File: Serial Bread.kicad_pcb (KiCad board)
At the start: 2 copper layers, 26 x 32 mm, 24 parts, among them J1 USB_C_Receptacle_USB2.0, J2 Conn_02x04_Top_Bottom, SW1 SW_SPDT, U1 CH340C, U2 AP2112K-3.3

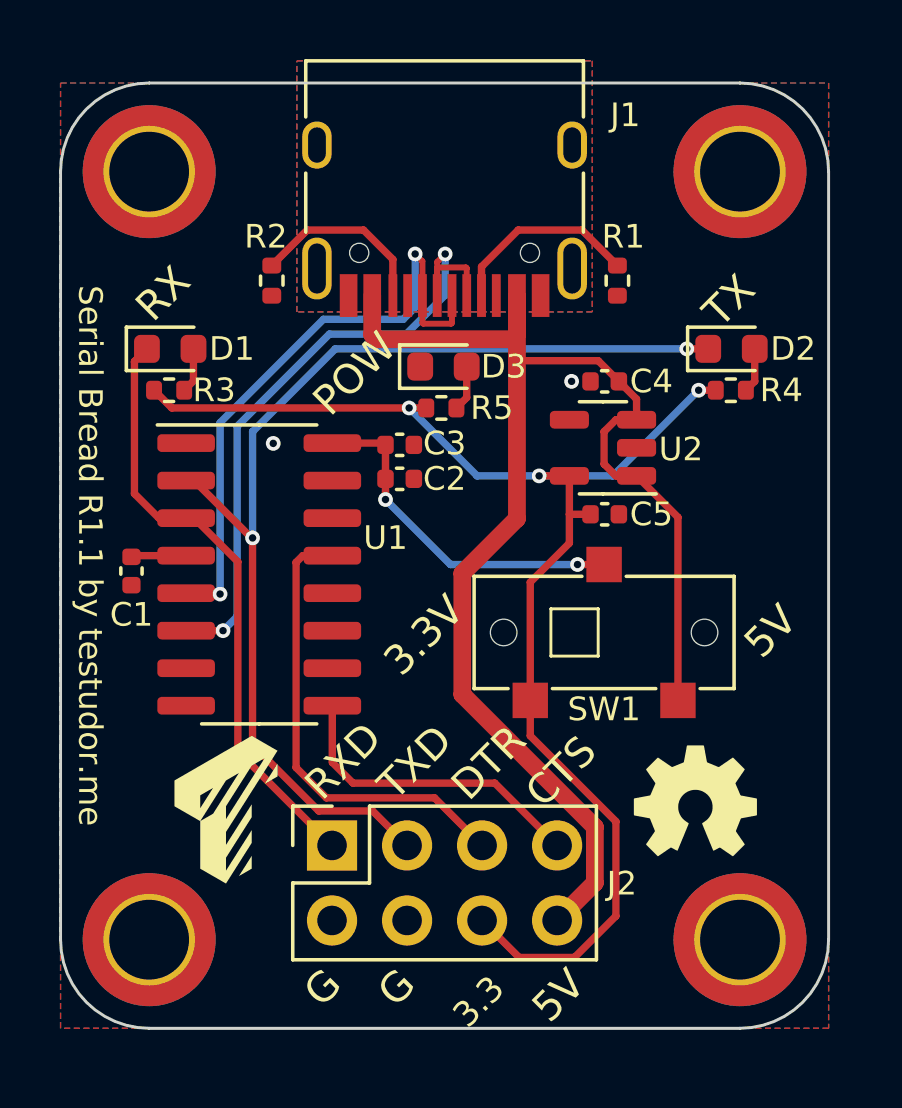
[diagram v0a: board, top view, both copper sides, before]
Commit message: Revert "Initial commit R1.1"
This reverts commit dbca94149cb8df2c718ea664c1760d3caefabc82.
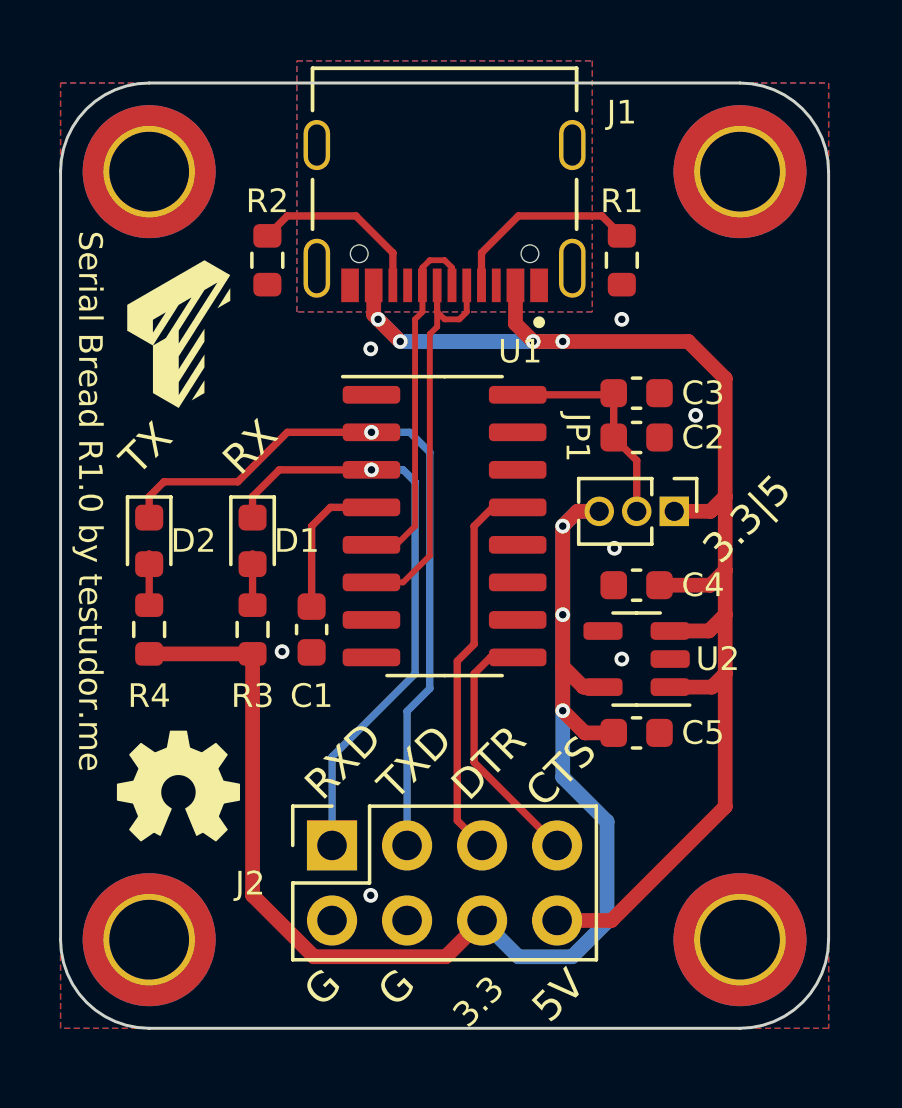
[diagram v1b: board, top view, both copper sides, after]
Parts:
- removed D3: LED RED, LED_SMD:LED_0603_1608Metric
- removed R5: 1k, Resistor_SMD:R_0402_1005Metric
- removed SW1: SW_SPDT, Custom_Switches:CL-SB-12B-02T
- added JP1: Jumper_3_Open, Connector_PinHeader_1.27mm:PinHeader_1x03_P1.27mm_Vertical, F.Cu at (167.8, 90.5)
- C1, C2, C3, C4, C5: footprint Capacitor_SMD:C_0402_1005Metric -> Capacitor_SMD:C_0603_1608Metric
- J1: value USB_C_Receptacle_USB2.0 -> TYPE-C-31-M-12; footprint Connector_USB:USB_C_Receptacle_HRO_TYPE-C-31-M-12 -> SnapEDA Library:HRO_TYPE-C-31-M-12
- R1, R2, R3, R4: footprint Resistor_SMD:R_0402_1005Metric -> Resistor_SMD:R_0603_1608Metric
- moved R4 21.3 mm to (150.0, 94.5), turned to 90 degrees
- moved D2 20.8 mm to (150.0, 91.5), turned to -90 degrees
- moved REF** 17.5 mm to (151.0, 100.0)
- moved REF** 16.2 mm to (151.0, 84.5)
- moved R3 8.58 mm to (153.5, 94.5), turned to 90 degrees
- moved C3 8.21 mm to (166.5, 86.5)
- moved C2 8.14 mm to (166.5, 88.0)
- moved C5 7.48 mm to (166.5, 98.0)
- moved U2 7.24 mm to (166.5, 95.5)
- moved D1 7.07 mm to (153.5, 91.5), turned to -90 degrees
- moved C4 6.98 mm to (166.5, 93.0)
- moved U1 6.48 mm to (160.0, 91.0)
- moved C1 6.41 mm to (155.5, 94.5)
- moved J1 1.05 mm to (160.0, 78.1)
- moved R1 0.71 mm to (166.0, 82.0)
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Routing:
- net /TXD: track 36.6 -> 25.0 mm, vias 2 -> 1
- net /D+: track 21.4 -> 12.4 mm, vias 2 -> 0
- net /D-: track 23.0 -> 14.6 mm, vias 2 -> 0
- net +3.3V: track 46.0 -> 52.9 mm
- net VCC: track 11.9 -> 7.60 mm, vias 2 -> 0
- net Net-(C1-Pad2): track 1.81 -> 5.01 mm
- net /DTR: track 15.7 -> 13.1 mm
- net /CTS: track 10.7 -> 8.68 mm
- net Net-(D3-A): track 1.54 -> 0.00 mm
- net +5V: track 49.1 -> 48.3 mm, vias 0 -> 4
- net /RXD: vias 0 -> 1
- net GND: vias 2 -> 7
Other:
- board text added: "3.3|5"
- board text added: "Serial Bread R1.0 by testudor.me"
- board text removed: "3.3V"
- board text removed: "POW"
- board text removed: "Serial Bread R1.1 by testudor.me"

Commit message: Initial commit R1.1
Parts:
- removed JP1: Jumper_3_Open, Connector_PinHeader_1.27mm:PinHeader_1x03_P1.27mm_Vertical
- added D3: LED RED, LED_SMD:LED_0603_1608Metric, F.Cu at (160.0, 85.6)
- added R5: 1k, Resistor_SMD:R_0402_1005Metric, F.Cu at (159.9, 87.0)
- added SW1: SW_SPDT, Custom_Switches:CL-SB-12B-02T, F.Cu at (165.4, 94.6)
- C1, C2, C3, C4, C5: footprint Capacitor_SMD:C_0603_1608Metric -> Capacitor_SMD:C_0402_1005Metric
- J1: value TYPE-C-31-M-12 -> USB_C_Receptacle_USB2.0; footprint SnapEDA Library:HRO_TYPE-C-31-M-12 -> Connector_USB:USB_C_Receptacle_HRO_TYPE-C-31-M-12
- R1, R2, R3, R4: footprint Resistor_SMD:R_0603_1608Metric -> Resistor_SMD:R_0402_1005Metric
- moved R4 21.3 mm to (169.7, 86.4), turned to 0 degrees
- moved D2 20.8 mm to (169.7, 85.0), turned to 0 degrees
- moved REF** 17.5 mm to (168.5, 100.5)
- moved REF** 16.2 mm to (152.6, 100.6)
- moved R3 8.58 mm to (150.7, 86.4), turned to 0 degrees
- moved C3 8.21 mm to (158.5, 88.2)
- moved C2 8.14 mm to (158.5, 89.4)
- moved C5 7.48 mm to (165.4, 90.6)
- moved U2 7.24 mm to (165.4, 88.3)
- moved D1 7.07 mm to (150.7, 85.0), turned to 0 degrees
- moved C4 6.98 mm to (165.4, 86.1)
- moved U1 6.48 mm to (153.7, 92.6)
- moved C1 6.41 mm to (149.4, 92.5)
- moved J1 1.05 mm to (160.0, 79.2)
- moved R1 0.71 mm to (165.8, 82.7)
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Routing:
- net /TXD: track 25.0 -> 36.6 mm, vias 1 -> 2
- net /D+: track 12.4 -> 21.4 mm, vias 0 -> 2
- net /D-: track 14.6 -> 23.0 mm, vias 0 -> 2
- net +3.3V: track 52.9 -> 46.0 mm
- net VCC: track 7.60 -> 11.9 mm, vias 0 -> 2
- net Net-(U1-V3): track 5.01 -> 1.81 mm
- net /DTR: track 13.1 -> 15.7 mm
- net /CTS: track 8.68 -> 10.7 mm
- net Net-(D3-A): track 0.00 -> 1.54 mm
- net +5V: track 48.3 -> 49.1 mm, vias 4 -> 0
- net /RXD: vias 1 -> 0
- net GND: vias 7 -> 2
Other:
- board text added: "3.3V"
- board text added: "POW"
- board text added: "Serial Bread R1.1 by testudor.me"
- board text removed: "3.3|5"
- board text removed: "Serial Bread R1.0 by testudor.me"

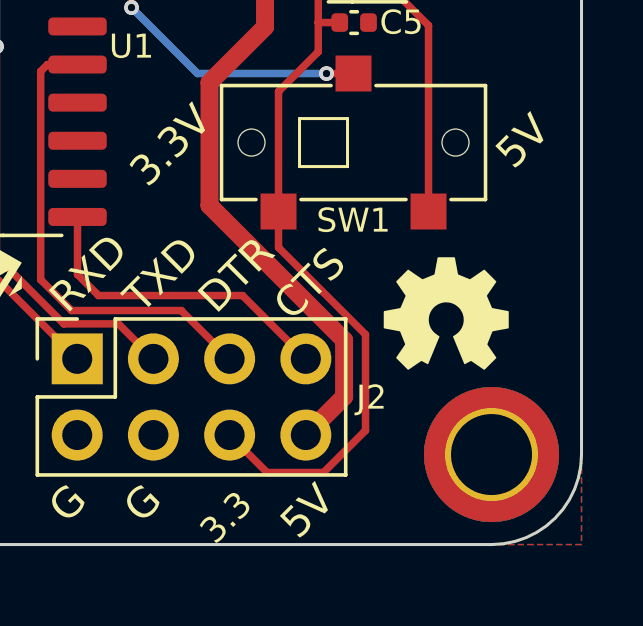
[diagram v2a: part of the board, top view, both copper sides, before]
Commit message: Fixed missing OSHW silk
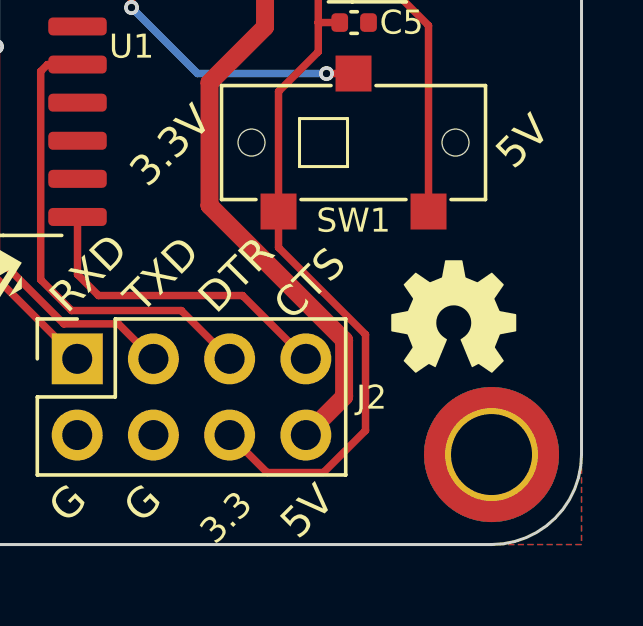
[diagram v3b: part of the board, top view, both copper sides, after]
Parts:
- moved REF** 0.27 mm to (168.8, 100.6)
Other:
- board text added: "PCB3D_BR_SERIAL-BREAD"
- board text added: "PCB3D_TL_SERIAL-BREAD"

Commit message: Revert "Fixed missing OSHW silk"
This reverts commit 2a56d455a99e7c22cc2508ea68d32a0d58d2fe36.
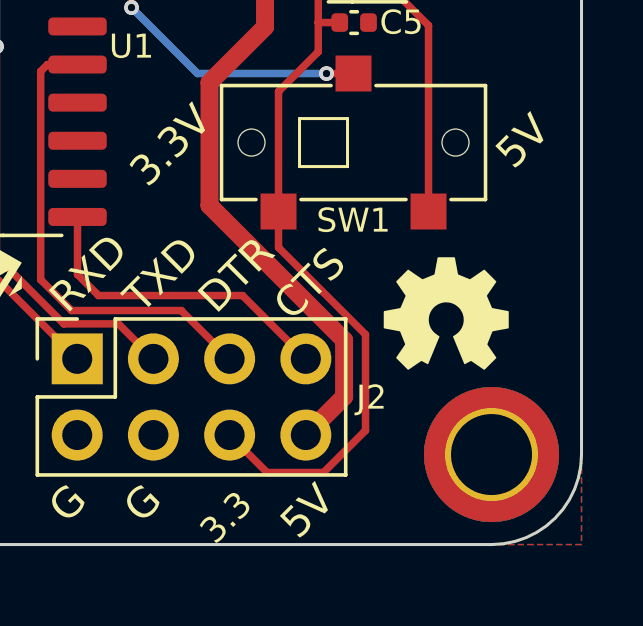
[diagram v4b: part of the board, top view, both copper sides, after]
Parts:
- moved REF** 0.27 mm to (168.5, 100.5)
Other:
- board text removed: "PCB3D_BR_SERIAL-BREAD"
- board text removed: "PCB3D_TL_SERIAL-BREAD"
